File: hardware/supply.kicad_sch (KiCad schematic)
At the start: 13 parts

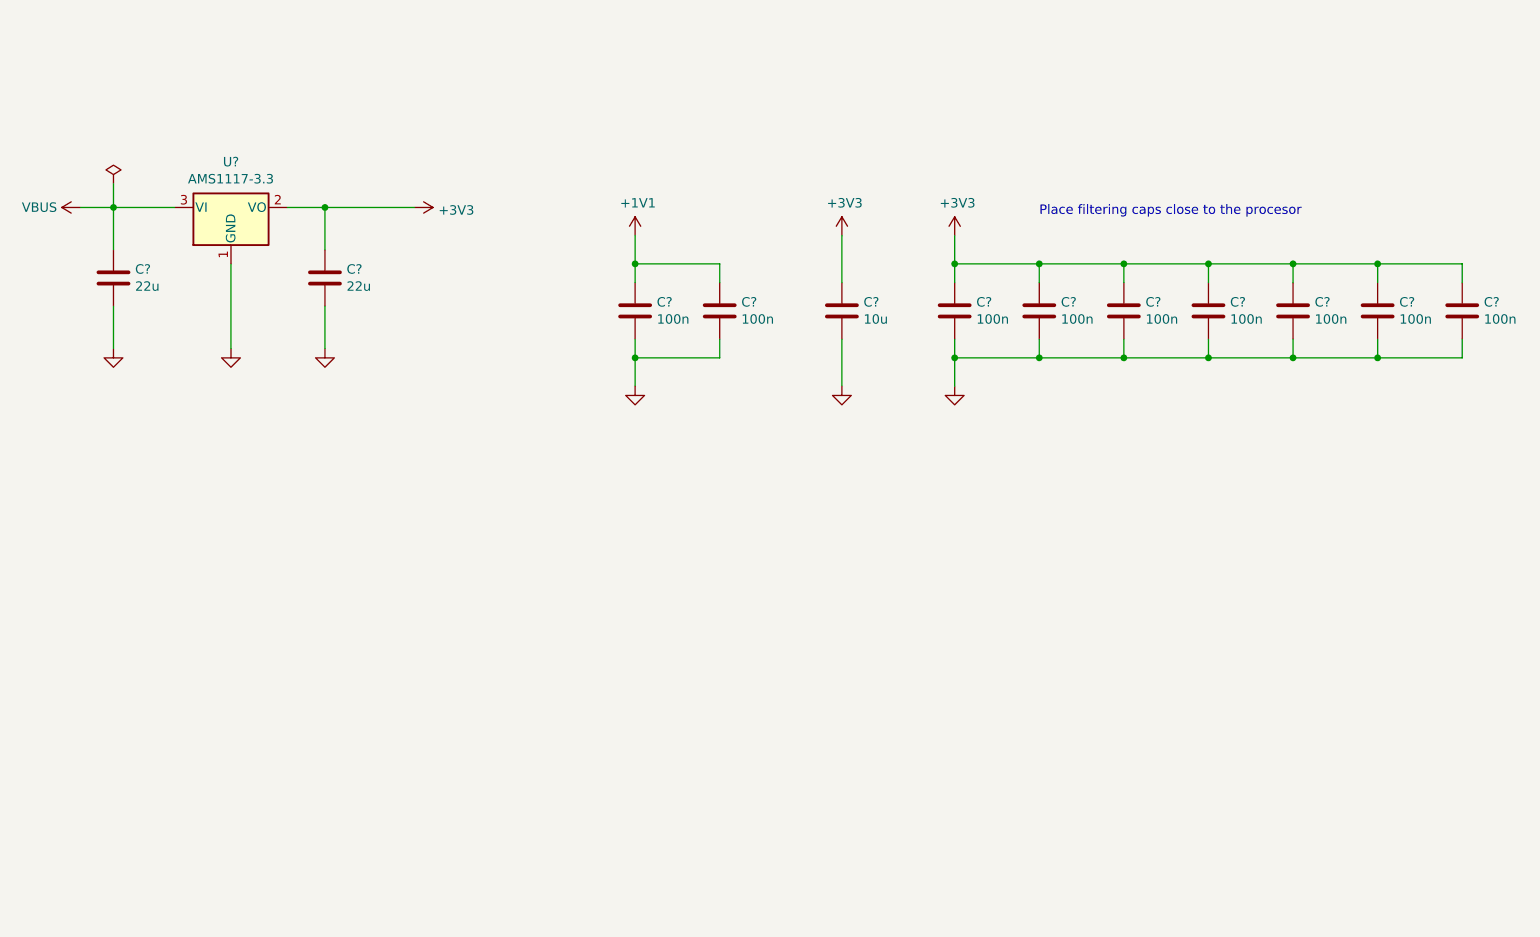
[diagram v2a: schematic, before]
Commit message: hw: Adjust power supply schem
- Replace 22u caps for 10u caps, to have more common parts
- Adjust schematic look and feel
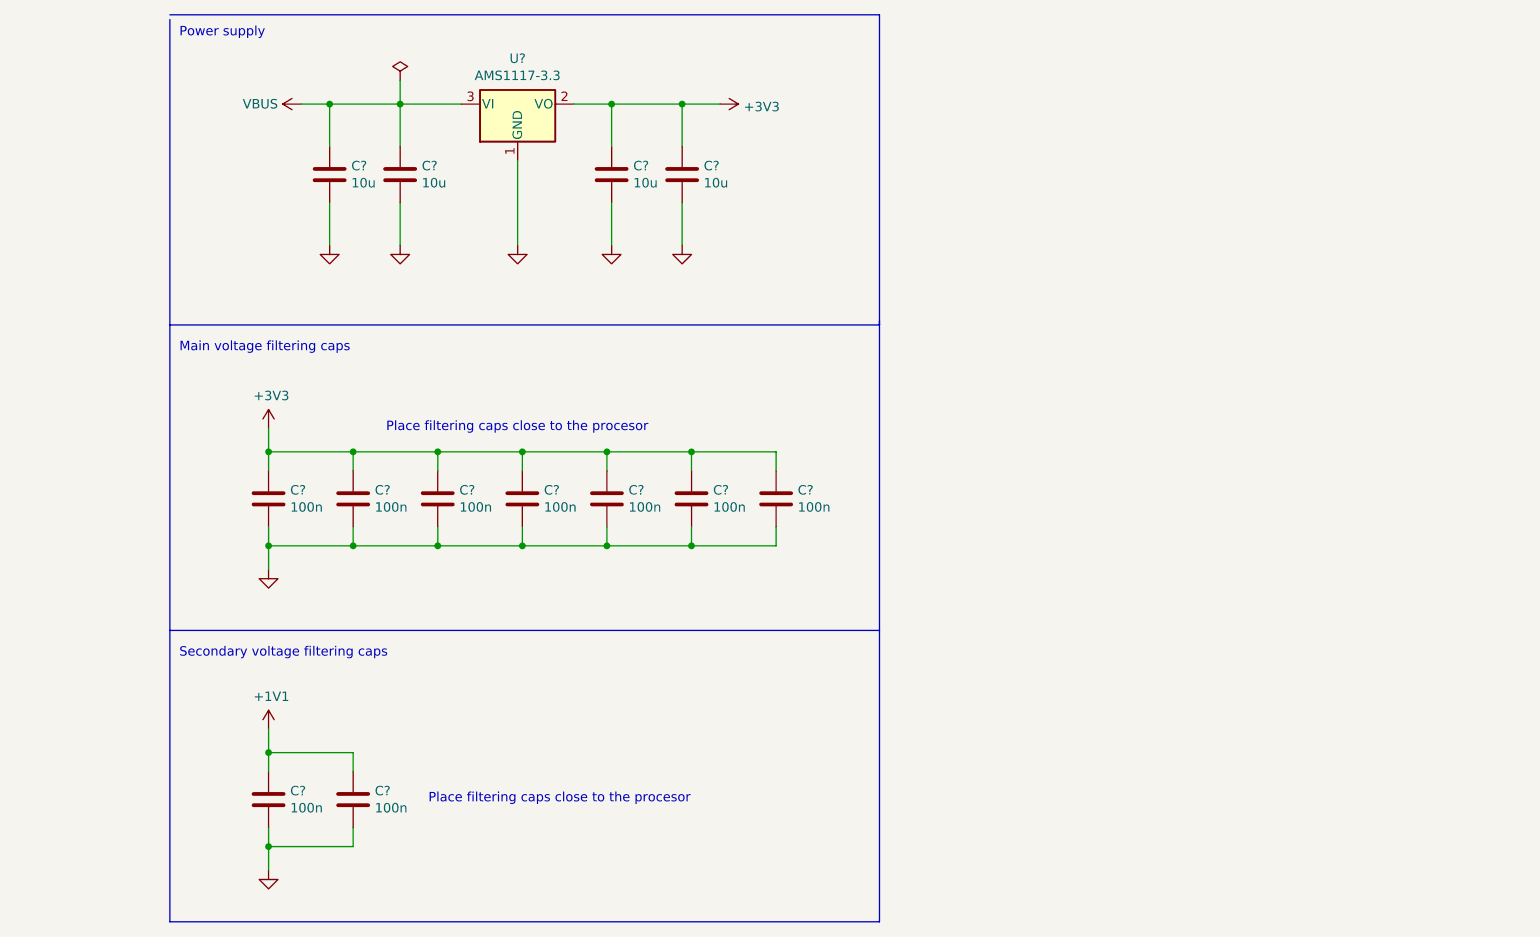
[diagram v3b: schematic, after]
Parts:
- removed C? (x2): 22u, Capacitor_SMD:C_1206_3216Metric_Pad1.33x1.80mm_HandSolder, symbol Device:C
- removed C?: 10u, Capacitor_SMD:C_1206_3216Metric_Pad1.33x1.80mm_HandSolder, symbol Device:C
- added C? (x4): 10u, Capacitor_SMD:C_1206_3216Metric_Pad1.33x1.80mm_HandSolder, symbol Device:C
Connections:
- net +3V3: now also C?.1, C?.1
- net GND: now also C?.2, C?.2, C?.2, C?.2
- net VBUS: now also C?.1, C?.1
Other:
- note added: "Main voltage filtering caps"
- note added: "Power supply"
- note added: "Secondary voltage filtering caps"
- moved on the sheet: C?, U?

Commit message: hw: Add the title block informations
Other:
- company: (none) -> Jan Krejčí
- title: (none) -> Pico probe
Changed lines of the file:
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@@
 (kicad_sch (version 20211123) (generator eeschema)
   (paper "A4")
+  (title_block
+    (title "Pico probe")
+    (date "2022-04-03")
+    (rev "22.04")
+    (company "Jan Krejčí")
+  )
   (junction (at 166.37 39.37) (diameter 0) (color 0 0 0 0)
   )
